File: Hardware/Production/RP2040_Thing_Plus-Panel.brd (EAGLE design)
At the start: 106.7 x 203.2 mm, 1590 parts, among them J1 SWD, J10 USB C, J11 microSD, J14 SWD, J15 Qwiic, J17 USB C, J18 microSD, J2 Qwiic, J21 SWD, J22 Qwiic, J24 USB C, J25 microSD, J28 SWD, J29 Qwiic, J3 Qwiic, J31 USB C, J32 microSD, J35 SWD, J36 Qwiic, J38 USB C, J39 microSD, J42 SWD, J43 Qwiic, J45 USB C, J46 microSD, J49 SWD, J5 USB C, J50 Qwiic, J52 USB C, J53 microSD, J56 SWD, J57 Qwiic, J59 USB C, J6 microSD, J60 microSD, J63 SWD, J64 Qwiic, J66 USB C, J67 microSD, J70 SWD, J71 Qwiic, J73 USB C, J74 microSD, J77 SWD, J78 Qwiic, J80 USB C, J81 microSD, J84 SWD, Q1 20V/4.2A/52mΩ/1.4W, Q10 20V/4.2A/52mΩ/1.4W, Q11 20V/4.2A/52mΩ/1.4W, Q12 20V/4.2A/52mΩ/1.4W, Q2 20V/4.2A/52mΩ/1.4W, Q3 20V/4.2A/52mΩ/1.4W, Q4 20V/4.2A/52mΩ/1.4W, Q5 20V/4.2A/52mΩ/1.4W, Q6 20V/4.2A/52mΩ/1.4W, Q7 20V/4.2A/52mΩ/1.4W, Q8 20V/4.2A/52mΩ/1.4W, Q9 20V/4.2A/52mΩ/1.4W, U1 W25QXX128MBIT, U10 WS2812-2020, U11 3.3V, U12 MCP73831, U13 W25QXX128MBIT, U14 RP2040, U15 MAX17048, U16 WS2812-2020, U17 3.3V, U18 MCP73831, U19 W25QXX128MBIT, U2 MAX17048, U20 RP2040, U21 MAX17048, U22 WS2812-2020, U23 3.3V, U24 MCP73831, U25 W25QXX128MBIT, U26 RP2040, U27 MAX17048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

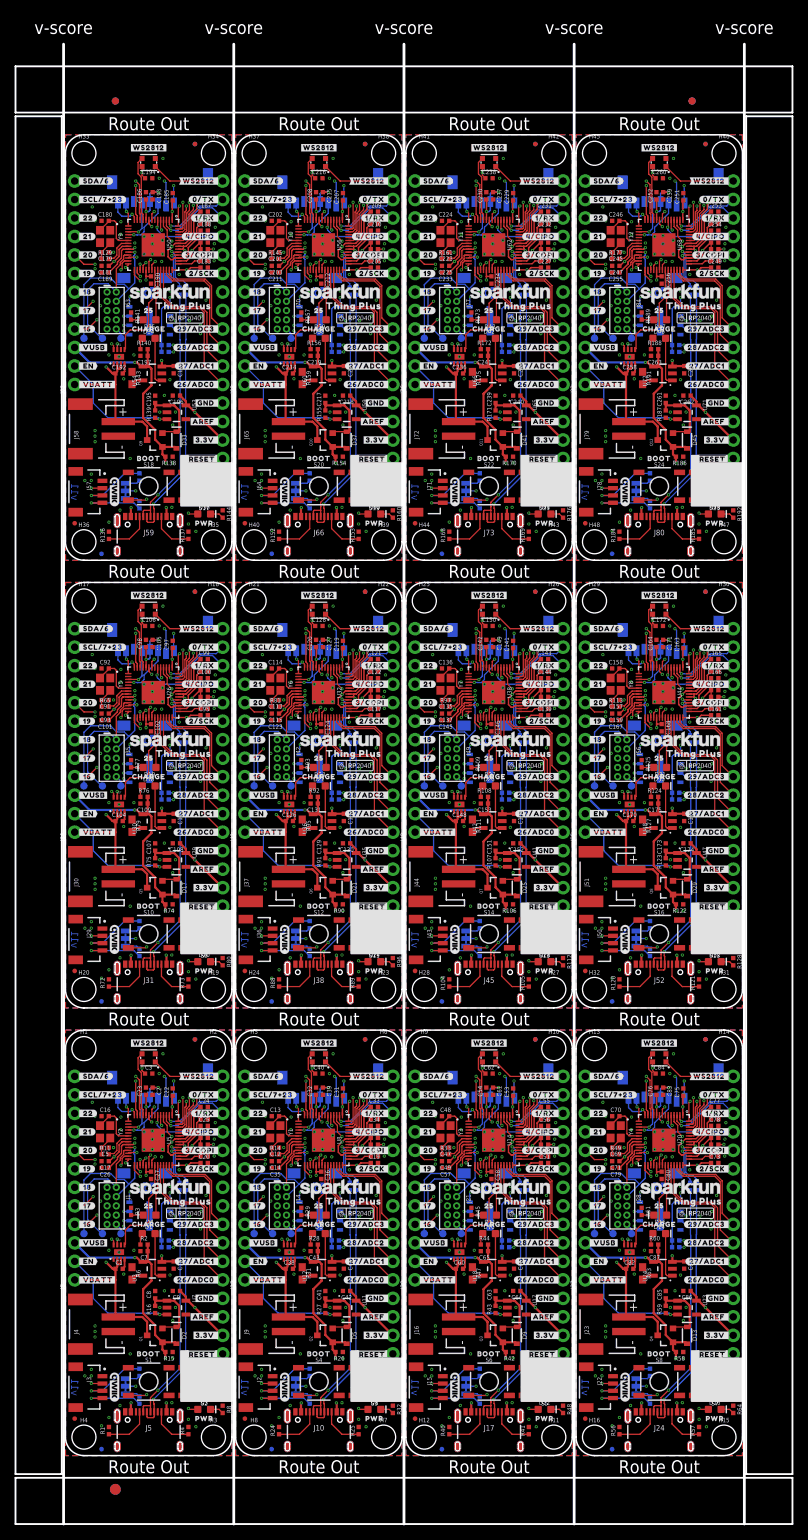
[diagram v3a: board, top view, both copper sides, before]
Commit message: Update RP2040 Logo
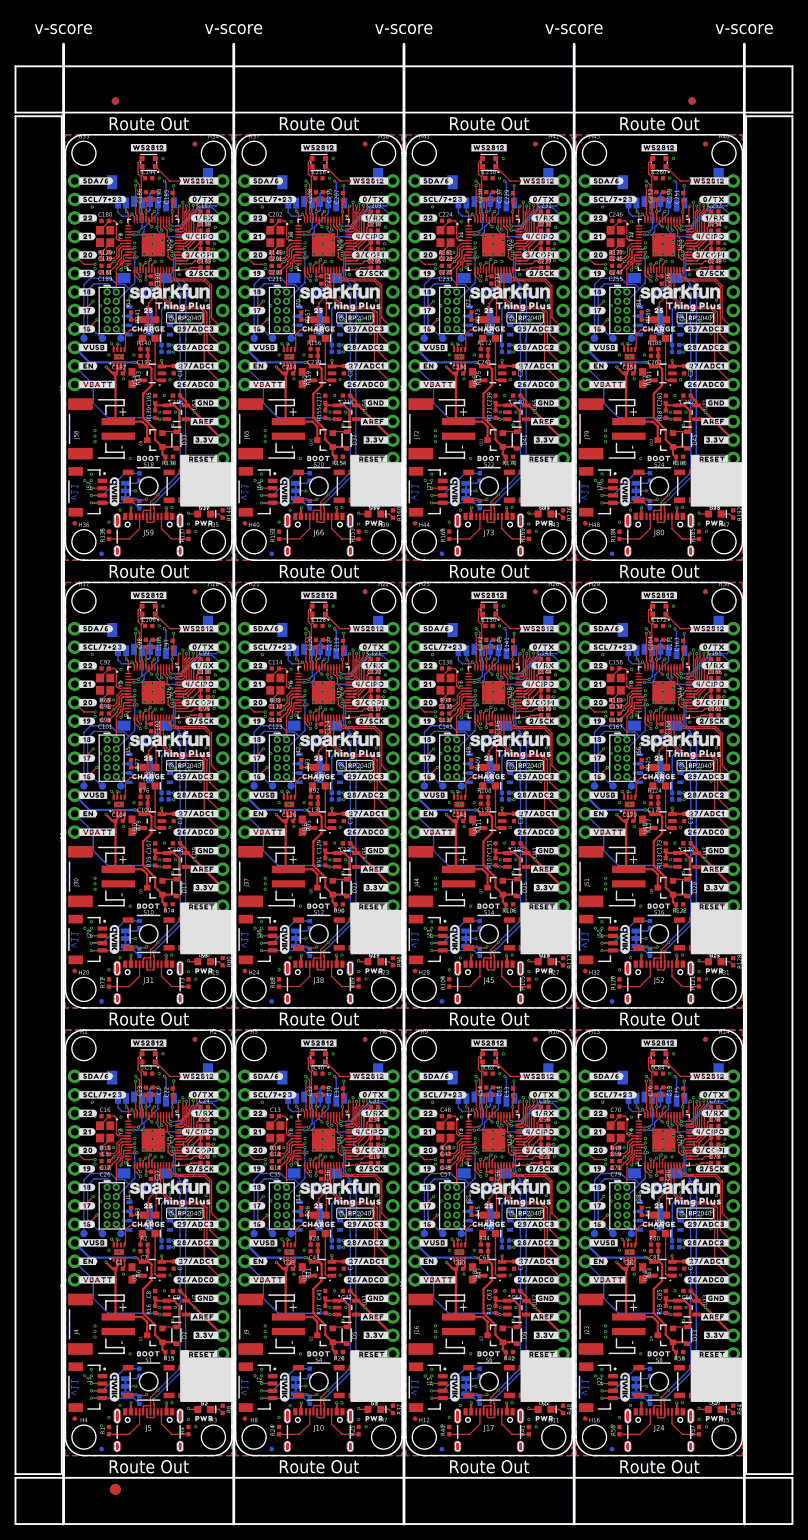
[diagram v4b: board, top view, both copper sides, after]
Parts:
- moved U$365 1.15 mm to (29.2, 75.9)
- moved U$426 1.15 mm to (52.6, 75.9)
- moved U$609 1.15 mm to (29.2, 137.4)
- moved U$670 1.15 mm to (52.6, 137.4)
- moved U$304 1.15 mm to (5.84, 75.9)
- moved U$548 1.15 mm to (5.84, 137.4)
- moved U$487 1.15 mm to (75.9, 75.9)
- moved U$731 1.15 mm to (75.9, 137.4)
- moved U$121 1.15 mm to (29.2, 14.5)
- moved U$182 1.15 mm to (52.6, 14.5)
- moved U$30 1.15 mm to (5.84, 14.5)
- moved U$243 1.15 mm to (75.9, 14.5)
- moved U$242 0.77 mm to (76.5, 17.1)
- moved U$486 0.77 mm to (76.5, 78.6)
- moved U$730 0.77 mm to (76.5, 140.1)
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
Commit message: Added ARM DevSummit Logo
Removed logos from bottom of PCB and replaced with ARM DevSummit logo.
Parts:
- removed U$709: (no value), output:#17_#0
- removed U$710: (no value), output:#16_#0
- removed U$711: (no value), output:#VUSB_#0
- removed U$712: (no value), output:#EN_#0
- removed U$713: (no value), output:#VBATT_#0
- removed U$714: (no value), output:#SCL_#0
- removed U$715: (no value), output:#SDA_#0
- removed U$716: (no value), output:#_#RESET##0
- removed U$717: (no value), output:#_3#3V#0
- removed U$718: (no value), output:#_AREF#0
- removed U$719: (no value), output:#_GND#0
- removed U$720: (no value), output:#_26#ADC0#0
- removed U$721: (no value), output:#_27#ADC1#0
- removed U$722: (no value), output:#_28#ADC2#0
- removed U$723: (no value), output:#_29#ADC3#0
- removed U$724, U$725: (no value), output:#_NC#0
- removed U$726: (no value), output:PWR0
- removed U$727: (no value), output:#I�C#0
- removed U$728: (no value), SparkFun-Aesthetics:SFE_LOGO_NAME_.1
- removed U$729: (no value), output:THING_PLUS_0
- removed U$730: (no value), output:THING_PLUS0
- removed U$731: (no value), RP2040:RP2040_20
- removed U$732: (no value), RP2040:RP2040_10
- U$100: device output:#16_#0 -> output:#VBATT_#0
- U$101: device output:#VUSB_#0 -> output:#SCL_#0
- U$102: device output:#EN_#0 -> output:#SDA_#0
- U$103: device output:#VBATT_#0 -> output:#_#RESET##0
- U$104: device output:#SCL_#0 -> output:#_3#3V#0
- U$105: device output:#SDA_#0 -> output:#_AREF#0
- U$106: device output:#_#RESET##0 -> output:#_GND#0
- U$107: device output:#_3#3V#0 -> output:#_26#ADC0#0
- U$108: device output:#_AREF#0 -> output:#_27#ADC1#0
- U$109: device output:#_GND#0 -> output:#_28#ADC2#0
- U$110: device output:#_26#ADC0#0 -> output:#_29#ADC3#0
- U$111: device output:#_27#ADC1#0 -> output:#_NC#0
- U$112: device output:#_28#ADC2#0 -> output:#_NC#0
- U$113: device output:#_29#ADC3#0 -> output:PWR0
- U$114: device output:#_NC#0 -> output:#I�C#0
- U$115: device output:#_NC#0 -> SparkFun-Aesthetics:SFE_LOGO_NAME_.1
- U$116: device output:PWR0 -> output:THING_PLUS_0
- U$117: device output:#I�C#0 -> RP2040:RP2040_10
- U$118: device SparkFun-Aesthetics:SFE_LOGO_NAME_.1 -> ARM1848_DevSummit_2021_Logos_ST3_Stacked#black#jpg (3):ARM1848_DEVSUMMIT_2021_LOGOS_ST3_STACKED#BLACK#JPG
- U$119: device output:THING_PLUS_0 -> output:#_16#0
- U$120: device output:THING_PLUS0 -> output:#_17#0
- U$121: device RP2040:RP2040_20 -> output:#_18#0
- U$122: device RP2040:RP2040_10 -> output:#_19#0
- U$123: device output:#_16#0 -> output:#_20#0
- U$124: device output:#_17#0 -> output:#_21#0
- U$125: device output:#_18#0 -> output:#_22#0
- U$126: device output:#_19#0 -> output:#WS2812_#0
- U$127: device output:#_20#0 -> output:#0#TX_#0
- U$128: device output:#_21#0 -> output:#1#RX_#0
- U$129: device output:#_22#0 -> output:#4#CIPO_#0
- U$130: device output:#WS2812_#0 -> output:#3#COPI_#0
- U$131: device output:#0#TX_#0 -> output:#2#SCK_#0
- U$132: device output:#1#RX_#0 -> output:#_SCL#7#23#0
- U$133: device output:#4#CIPO_#0 -> output:#_SDA#6#0
- U$134: device output:#3#COPI_#0 -> output:#29#ADC3_#0
- U$135: device output:#2#SCK_#0 -> output:#28#ADC2_#0
- U$136: device output:#_SCL#7#23#0 -> output:#27#ADC1_#0
- U$137: device output:#_SDA#6#0 -> output:#26#ADC0_#0
- U$138: device output:#29#ADC3_#0 -> output:#_VUSB#0
- U$139: device output:#28#ADC2_#0 -> output:#_EN#0
- U$140: device output:#27#ADC1_#0 -> output:#_VBATT#0
- U$141: device output:#26#ADC0_#0 -> output:#GND_#0
- U$142: device output:#_VUSB#0 -> output:#AREF_#0
- U$143: device output:#_EN#0 -> output:#3#3V_#0
- U$144: device output:#_VBATT#0 -> output:##RESET##0
- U$145: device output:#GND_#0 -> output:#WS2812#0
- U$146: device output:#AREF_#0 -> SparkFun-Aesthetics:QWIIC_4MM
- U$147: device output:#3#3V_#0 -> output:250
- U$148: device output:##RESET##0 -> output:CHARGE0
- U$149: device output:#WS2812#0 -> output:BOOT0
- U$150: device SparkFun-Aesthetics:QWIIC_4MM -> output:#22_#0
- U$151: device SparkFun-Aesthetics:SFE_LOGO_NAME_FLAME_.1 -> output:#21_#0
- U$152: device output:250 -> output:#20_#0
- U$153: device output:CHARGE0 -> output:#19_#0
- U$154: device output:BOOT0 -> output:#18_#0
- U$155: device output:#22_#0 -> output:#17_#0
- U$156: device output:#21_#0 -> output:#16_#0
- U$157: device output:#20_#0 -> output:#VUSB_#0
- U$158: device output:#19_#0 -> output:#EN_#0
- U$159: device output:#18_#0 -> output:#VBATT_#0
- U$160: device output:#17_#0 -> output:#SCL_#0
- U$161: device output:#16_#0 -> output:#SDA_#0
- U$162: device output:#VUSB_#0 -> output:#_#RESET##0
- U$163: device output:#EN_#0 -> output:#_3#3V#0
- U$164: device output:#VBATT_#0 -> output:#_AREF#0
- U$165: device output:#SCL_#0 -> output:#_GND#0
- U$166: device output:#SDA_#0 -> output:#_26#ADC0#0
- U$167: device output:#_#RESET##0 -> output:#_27#ADC1#0
- U$168: device output:#_3#3V#0 -> output:#_28#ADC2#0
- U$169: device output:#_AREF#0 -> output:#_29#ADC3#0
- U$170: device output:#_GND#0 -> output:#_NC#0
- U$171: device output:#_26#ADC0#0 -> output:#_NC#0
- U$172: device output:#_27#ADC1#0 -> output:PWR0
- U$173: device output:#_28#ADC2#0 -> output:#I�C#0
- U$174: device output:#_29#ADC3#0 -> SparkFun-Aesthetics:SFE_LOGO_NAME_.1
- U$175: device output:#_NC#0 -> output:THING_PLUS_0
- U$176: device output:#_NC#0 -> RP2040:RP2040_10
- U$177: device output:PWR0 -> ARM1848_DevSummit_2021_Logos_ST3_Stacked#black#jpg (3):ARM1848_DEVSUMMIT_2021_LOGOS_ST3_STACKED#BLACK#JPG
- U$178: device output:#I�C#0 -> output:#_16#0
- U$179: device SparkFun-Aesthetics:SFE_LOGO_NAME_.1 -> output:#_17#0
- U$180: device output:THING_PLUS_0 -> output:#_18#0
- U$181, U$44: device output:THING_PLUS0 -> output:#_19#0
- U$182: device RP2040:RP2040_20 -> output:#_20#0
- U$183: device RP2040:RP2040_10 -> output:#_21#0
- U$184: device output:#_16#0 -> output:#_22#0
- U$185: device output:#_17#0 -> output:#WS2812_#0
- U$186: device output:#_18#0 -> output:#0#TX_#0
- U$187: device output:#_19#0 -> output:#1#RX_#0
- U$188: device output:#_20#0 -> output:#4#CIPO_#0
- U$189: device output:#_21#0 -> output:#3#COPI_#0
- U$190: device output:#_22#0 -> output:#2#SCK_#0
- U$191: device output:#WS2812_#0 -> output:#_SCL#7#23#0
- U$192: device output:#0#TX_#0 -> output:#_SDA#6#0
- U$193: device output:#1#RX_#0 -> output:#29#ADC3_#0
- U$194: device output:#4#CIPO_#0 -> output:#28#ADC2_#0
- U$195: device output:#3#COPI_#0 -> output:#27#ADC1_#0
- U$196: device output:#2#SCK_#0 -> output:#26#ADC0_#0
- U$197: device output:#_SCL#7#23#0 -> output:#_VUSB#0
- U$198: device output:#_SDA#6#0 -> output:#_EN#0
- U$199: device output:#29#ADC3_#0 -> output:#_VBATT#0
- U$200: device output:#28#ADC2_#0 -> output:#GND_#0
- U$201: device output:#27#ADC1_#0 -> output:#AREF_#0
- U$202: device output:#26#ADC0_#0 -> output:#3#3V_#0
- U$203: device output:#_VUSB#0 -> output:##RESET##0
- U$204: device output:#_EN#0 -> output:#WS2812#0
- U$205: device output:#_VBATT#0 -> SparkFun-Aesthetics:QWIIC_4MM
- U$206: device output:#GND_#0 -> output:250
- U$207: device output:#AREF_#0 -> output:CHARGE0
- U$208: device output:#3#3V_#0 -> output:BOOT0
- U$209: device output:##RESET##0 -> output:#22_#0
- U$210: device output:#WS2812#0 -> output:#21_#0
- U$211: device SparkFun-Aesthetics:QWIIC_4MM -> output:#20_#0
- U$212: device SparkFun-Aesthetics:SFE_LOGO_NAME_FLAME_.1 -> output:#19_#0
- U$213: device output:250 -> output:#18_#0
- U$214: device output:CHARGE0 -> output:#17_#0
- U$215: device output:BOOT0 -> output:#16_#0
- U$216: device output:#22_#0 -> output:#VUSB_#0
- U$217: device output:#21_#0 -> output:#EN_#0
- U$218: device output:#20_#0 -> output:#VBATT_#0
- U$219: device output:#19_#0 -> output:#SCL_#0
- U$220: device output:#18_#0 -> output:#SDA_#0
- U$221: device output:#17_#0 -> output:#_#RESET##0
- U$222: device output:#16_#0 -> output:#_3#3V#0
- U$223: device output:#VUSB_#0 -> output:#_AREF#0
- U$224: device output:#EN_#0 -> output:#_GND#0
- U$225: device output:#VBATT_#0 -> output:#_26#ADC0#0
- U$226: device output:#SCL_#0 -> output:#_27#ADC1#0
- U$227: device output:#SDA_#0 -> output:#_28#ADC2#0
- U$228: device output:#_#RESET##0 -> output:#_29#ADC3#0
- U$229: device output:#_3#3V#0 -> output:#_NC#0
- U$230: device output:#_AREF#0 -> output:#_NC#0
- U$231: device output:#_GND#0 -> output:PWR0
- U$232: device output:#_26#ADC0#0 -> output:#I�C#0
- U$233: device output:#_27#ADC1#0 -> SparkFun-Aesthetics:SFE_LOGO_NAME_.1
- U$234: device output:#_28#ADC2#0 -> output:THING_PLUS_0
- U$235: device output:#_29#ADC3#0 -> RP2040:RP2040_10
- U$236: device output:#_NC#0 -> ARM1848_DevSummit_2021_Logos_ST3_Stacked#black#jpg (3):ARM1848_DEVSUMMIT_2021_LOGOS_ST3_STACKED#BLACK#JPG
- U$237: device output:#_NC#0 -> output:#_16#0
- U$238: device output:PWR0 -> output:#_17#0
- U$239: device output:#I�C#0 -> output:#_18#0
- U$240: device SparkFun-Aesthetics:SFE_LOGO_NAME_.1 -> output:#_19#0
- U$241: device output:THING_PLUS_0 -> output:#_20#0
- U$242: device output:THING_PLUS0 -> output:#_21#0
- U$243: device RP2040:RP2040_20 -> output:#_22#0
- U$244: device RP2040:RP2040_10 -> output:#WS2812_#0
- U$245: device output:#_16#0 -> output:#0#TX_#0
- U$246: device output:#_17#0 -> output:#1#RX_#0
- U$247: device output:#_18#0 -> output:#4#CIPO_#0
- U$248: device output:#_19#0 -> output:#3#COPI_#0
- U$249: device output:#_20#0 -> output:#2#SCK_#0
- U$250: device output:#_21#0 -> output:#_SCL#7#23#0
- U$251: device output:#_22#0 -> output:#_SDA#6#0
- U$252: device output:#WS2812_#0 -> output:#29#ADC3_#0
- U$253: device output:#0#TX_#0 -> output:#28#ADC2_#0
- U$254: device output:#1#RX_#0 -> output:#27#ADC1_#0
- U$255: device output:#4#CIPO_#0 -> output:#26#ADC0_#0
- U$256: device output:#3#COPI_#0 -> output:#_VUSB#0
- U$257: device output:#2#SCK_#0 -> output:#_EN#0
- U$258: device output:#_SCL#7#23#0 -> output:#_VBATT#0
- U$259: device output:#_SDA#6#0 -> output:#GND_#0
- U$260: device output:#29#ADC3_#0 -> output:#AREF_#0
- U$261: device output:#28#ADC2_#0 -> output:#3#3V_#0
- U$262: device output:#27#ADC1_#0 -> output:##RESET##0
- U$263: device output:#26#ADC0_#0 -> output:#WS2812#0
- U$264: device output:#_VUSB#0 -> SparkFun-Aesthetics:QWIIC_4MM
- U$265: device output:#_EN#0 -> output:250
- U$266: device output:#_VBATT#0 -> output:CHARGE0
- U$267: device output:#GND_#0 -> output:BOOT0
- U$268: device output:#AREF_#0 -> output:#22_#0
- U$269: device output:#3#3V_#0 -> output:#21_#0
- U$270: device output:##RESET##0 -> output:#20_#0
- U$271: device output:#WS2812#0 -> output:#19_#0
- U$272: device SparkFun-Aesthetics:QWIIC_4MM -> output:#18_#0
- U$273: device SparkFun-Aesthetics:SFE_LOGO_NAME_FLAME_.1 -> output:#17_#0
- U$274: device output:250 -> output:#16_#0
- U$275: device output:CHARGE0 -> output:#VUSB_#0
- U$276: device output:BOOT0 -> output:#EN_#0
- U$277: device output:#22_#0 -> output:#VBATT_#0
- U$278: device output:#21_#0 -> output:#SCL_#0
- U$279: device output:#20_#0 -> output:#SDA_#0
- U$280: device output:#19_#0 -> output:#_#RESET##0
- U$281: device output:#18_#0 -> output:#_3#3V#0
- U$282: device output:#17_#0 -> output:#_AREF#0
- U$283: device output:#16_#0 -> output:#_GND#0
- U$284: device output:#VUSB_#0 -> output:#_26#ADC0#0
- U$285: device output:#EN_#0 -> output:#_27#ADC1#0
- U$286: device output:#VBATT_#0 -> output:#_28#ADC2#0
- U$287: device output:#SCL_#0 -> output:#_29#ADC3#0
- U$288: device output:#SDA_#0 -> output:#_NC#0
- U$289: device output:#_#RESET##0 -> output:#_NC#0
- U$290: device output:#_3#3V#0 -> output:PWR0
- U$291: device output:#_AREF#0 -> output:#I�C#0
- U$292: device output:#_GND#0 -> SparkFun-Aesthetics:SFE_LOGO_NAME_.1
- U$293: device output:#_26#ADC0#0 -> output:THING_PLUS_0
- U$294: device output:#_27#ADC1#0 -> RP2040:RP2040_10
- U$295: device output:#_28#ADC2#0 -> ARM1848_DevSummit_2021_Logos_ST3_Stacked#black#jpg (3):ARM1848_DEVSUMMIT_2021_LOGOS_ST3_STACKED#BLACK#JPG
- U$296: device output:#_29#ADC3#0 -> output:#_16#0
- U$297: device output:#_NC#0 -> output:#_17#0
- U$298: device output:#_NC#0 -> output:#_18#0
- U$299: device output:PWR0 -> output:#_19#0
- U$30: device RP2040:RP2040_20 -> ARM1848_DevSummit_2021_Logos_ST3_Stacked#black#jpg (3):ARM1848_DEVSUMMIT_2021_LOGOS_ST3_STACKED#BLACK#JPG
- U$300: device output:#I�C#0 -> output:#_20#0
- U$301: device SparkFun-Aesthetics:SFE_LOGO_NAME_.1 -> output:#_21#0
- U$302: device output:THING_PLUS_0 -> output:#_22#0
- U$303: device output:THING_PLUS0 -> output:#WS2812_#0
- U$304: device RP2040:RP2040_20 -> output:#0#TX_#0
- U$305: device RP2040:RP2040_10 -> output:#1#RX_#0
- U$306: device output:#_16#0 -> output:#4#CIPO_#0
- U$307: device output:#_17#0 -> output:#3#COPI_#0
- U$308: device output:#_18#0 -> output:#2#SCK_#0
- U$309: device output:#_19#0 -> output:#_SCL#7#23#0
- U$310: device output:#_20#0 -> output:#_SDA#6#0
- U$311: device output:#_21#0 -> output:#29#ADC3_#0
- U$312: device output:#_22#0 -> output:#28#ADC2_#0
- U$313: device output:#WS2812_#0 -> output:#27#ADC1_#0
- U$314: device output:#0#TX_#0 -> output:#26#ADC0_#0
- U$315: device output:#1#RX_#0 -> output:#_VUSB#0
- U$316: device output:#4#CIPO_#0 -> output:#_EN#0
- U$317: device output:#3#COPI_#0 -> output:#_VBATT#0
- U$318: device output:#2#SCK_#0 -> output:#GND_#0
- U$319: device output:#_SCL#7#23#0 -> output:#AREF_#0
- U$32: device SparkFun-Aesthetics:SFE_LOGO_NAME_FLAME_.1 -> output:#_17#0
- U$320: device output:#_SDA#6#0 -> output:#3#3V_#0
- U$321: device output:#29#ADC3_#0 -> output:##RESET##0
- U$322: device output:#28#ADC2_#0 -> output:#WS2812#0
- U$323: device output:#27#ADC1_#0 -> SparkFun-Aesthetics:QWIIC_4MM
- U$324: device output:#26#ADC0_#0 -> output:250
- U$325: device output:#_VUSB#0 -> output:CHARGE0
- U$326: device output:#_EN#0 -> output:BOOT0
- U$327: device output:#_VBATT#0 -> output:#22_#0
- U$328: device output:#GND_#0 -> output:#21_#0
- U$329: device output:#AREF_#0 -> output:#20_#0
- U$330: device output:#3#3V_#0 -> output:#19_#0
- U$331: device output:##RESET##0 -> output:#18_#0
- U$332: device output:#WS2812#0 -> output:#17_#0
- U$333: device SparkFun-Aesthetics:QWIIC_4MM -> output:#16_#0
- U$334: device SparkFun-Aesthetics:SFE_LOGO_NAME_FLAME_.1 -> output:#VUSB_#0
- U$335: device output:250 -> output:#EN_#0
- U$336: device output:CHARGE0 -> output:#VBATT_#0
- U$337: device output:BOOT0 -> output:#SCL_#0
- U$338: device output:#22_#0 -> output:#SDA_#0
- U$339: device output:#21_#0 -> output:#_#RESET##0
- U$340: device output:#20_#0 -> output:#_3#3V#0
- U$341: device output:#19_#0 -> output:#_AREF#0
- U$342: device output:#18_#0 -> output:#_GND#0
- U$343: device output:#17_#0 -> output:#_26#ADC0#0
- U$344: device output:#16_#0 -> output:#_27#ADC1#0
- U$345: device output:#VUSB_#0 -> output:#_28#ADC2#0
- U$346: device output:#EN_#0 -> output:#_29#ADC3#0
- U$347: device output:#VBATT_#0 -> output:#_NC#0
- U$348: device output:#SCL_#0 -> output:#_NC#0
- U$349: device output:#SDA_#0 -> output:PWR0
- U$350: device output:#_#RESET##0 -> output:#I�C#0
- U$351: device output:#_3#3V#0 -> SparkFun-Aesthetics:SFE_LOGO_NAME_.1
- U$352: device output:#_AREF#0 -> output:THING_PLUS_0
- U$353: device output:#_GND#0 -> RP2040:RP2040_10
- U$354: device output:#_26#ADC0#0 -> ARM1848_DevSummit_2021_Logos_ST3_Stacked#black#jpg (3):ARM1848_DEVSUMMIT_2021_LOGOS_ST3_STACKED#BLACK#JPG
- U$355: device output:#_27#ADC1#0 -> output:#_16#0
- U$356: device output:#_28#ADC2#0 -> output:#_17#0
- U$357: device output:#_29#ADC3#0 -> output:#_18#0
- U$358: device output:#_NC#0 -> output:#_19#0
- U$359: device output:#_NC#0 -> output:#_20#0
- U$360: device output:PWR0 -> output:#_21#0
- U$361: device output:#I�C#0 -> output:#_22#0
- U$362: device SparkFun-Aesthetics:SFE_LOGO_NAME_.1 -> output:#WS2812_#0
- U$363: device output:THING_PLUS_0 -> output:#0#TX_#0
- U$364: device output:THING_PLUS0 -> output:#1#RX_#0
- U$365: device RP2040:RP2040_20 -> output:#4#CIPO_#0
- U$366: device RP2040:RP2040_10 -> output:#3#COPI_#0
- U$367: device output:#_16#0 -> output:#2#SCK_#0
- U$368: device output:#_17#0 -> output:#_SCL#7#23#0
- U$369: device output:#_18#0 -> output:#_SDA#6#0
- U$370: device output:#_19#0 -> output:#29#ADC3_#0
- U$371: device output:#_20#0 -> output:#28#ADC2_#0
- U$372: device output:#_21#0 -> output:#27#ADC1_#0
- U$373: device output:#_22#0 -> output:#26#ADC0_#0
- U$374: device output:#WS2812_#0 -> output:#_VUSB#0
- U$375: device output:#0#TX_#0 -> output:#_EN#0
- U$376: device output:#1#RX_#0 -> output:#_VBATT#0
- U$377: device output:#4#CIPO_#0 -> output:#GND_#0
- U$378: device output:#3#COPI_#0 -> output:#AREF_#0
- U$379: device output:#2#SCK_#0 -> output:#3#3V_#0
- U$380: device output:#_SCL#7#23#0 -> output:##RESET##0
- U$381: device output:#_SDA#6#0 -> output:#WS2812#0
- U$382: device output:#29#ADC3_#0 -> SparkFun-Aesthetics:QWIIC_4MM
- U$383: device output:#28#ADC2_#0 -> output:250
- U$384: device output:#27#ADC1_#0 -> output:CHARGE0
- U$385: device output:#26#ADC0_#0 -> output:BOOT0
- U$386: device output:#_VUSB#0 -> output:#22_#0
- U$387: device output:#_EN#0 -> output:#21_#0
- U$388: device output:#_VBATT#0 -> output:#20_#0
- U$389: device output:#GND_#0 -> output:#19_#0
- U$390: device output:#AREF_#0 -> output:#18_#0
- U$391: device output:#3#3V_#0 -> output:#17_#0
- U$392: device output:##RESET##0 -> output:#16_#0
- U$393: device output:#WS2812#0 -> output:#VUSB_#0
- U$394: device SparkFun-Aesthetics:QWIIC_4MM -> output:#EN_#0
- U$395: device SparkFun-Aesthetics:SFE_LOGO_NAME_FLAME_.1 -> output:#VBATT_#0
- U$396: device output:250 -> output:#SCL_#0
- U$397: device output:CHARGE0 -> output:#SDA_#0
- U$398: device output:BOOT0 -> output:#_#RESET##0
- U$399: device output:#22_#0 -> output:#_3#3V#0
- U$400: device output:#21_#0 -> output:#_AREF#0
- U$401: device output:#20_#0 -> output:#_GND#0
- U$402: device output:#19_#0 -> output:#_26#ADC0#0
- U$403: device output:#18_#0 -> output:#_27#ADC1#0
- U$404: device output:#17_#0 -> output:#_28#ADC2#0
- U$405: device output:#16_#0 -> output:#_29#ADC3#0
- U$406: device output:#VUSB_#0 -> output:#_NC#0
- U$407: device output:#EN_#0 -> output:#_NC#0
- U$408: device output:#VBATT_#0 -> output:PWR0
- U$409: device output:#SCL_#0 -> output:#I�C#0
- U$410: device output:#SDA_#0 -> SparkFun-Aesthetics:SFE_LOGO_NAME_.1
- U$411: device output:#_#RESET##0 -> output:THING_PLUS_0
- U$412: device output:#_3#3V#0 -> RP2040:RP2040_10
- U$413: device output:#_AREF#0 -> ARM1848_DevSummit_2021_Logos_ST3_Stacked#black#jpg (3):ARM1848_DEVSUMMIT_2021_LOGOS_ST3_STACKED#BLACK#JPG
- U$414: device output:#_GND#0 -> output:#_16#0
- U$415: device output:#_26#ADC0#0 -> output:#_17#0
- U$416: device output:#_27#ADC1#0 -> output:#_18#0
- U$417: device output:#_28#ADC2#0 -> output:#_19#0
- U$418: device output:#_29#ADC3#0 -> output:#_20#0
- U$419: device output:#_NC#0 -> output:#_21#0
- U$420: device output:#_NC#0 -> output:#_22#0
- U$421: device output:PWR0 -> output:#WS2812_#0
- U$422: device output:#I�C#0 -> output:#0#TX_#0
- U$423: device SparkFun-Aesthetics:SFE_LOGO_NAME_.1 -> output:#1#RX_#0
- U$424: device output:THING_PLUS_0 -> output:#4#CIPO_#0
- U$425: device output:THING_PLUS0 -> output:#3#COPI_#0
- U$426: device RP2040:RP2040_20 -> output:#2#SCK_#0
- U$427: device RP2040:RP2040_10 -> output:#_SCL#7#23#0
- U$428: device output:#_16#0 -> output:#_SDA#6#0
- U$429: device output:#_17#0 -> output:#29#ADC3_#0
- U$43: device output:#_17#0 -> output:#_18#0
- U$430: device output:#_18#0 -> output:#28#ADC2_#0
- U$431: device output:#_19#0 -> output:#27#ADC1_#0
- U$432: device output:#_20#0 -> output:#26#ADC0_#0
- U$433: device output:#_21#0 -> output:#_VUSB#0
- U$434: device output:#_22#0 -> output:#_EN#0
- U$435: device output:#WS2812_#0 -> output:#_VBATT#0
- U$436: device output:#0#TX_#0 -> output:#GND_#0
- U$437: device output:#1#RX_#0 -> output:#AREF_#0
- U$438: device output:#4#CIPO_#0 -> output:#3#3V_#0
- U$439: device output:#3#COPI_#0 -> output:##RESET##0
- U$440: device output:#2#SCK_#0 -> output:#WS2812#0
- U$441: device output:#_SCL#7#23#0 -> SparkFun-Aesthetics:QWIIC_4MM
- U$442: device output:#_SDA#6#0 -> output:250
- U$443: device output:#29#ADC3_#0 -> output:CHARGE0
- U$444: device output:#28#ADC2_#0 -> output:BOOT0
- U$445: device output:#27#ADC1_#0 -> output:#22_#0
- U$446: device output:#26#ADC0_#0 -> output:#21_#0
- U$447: device output:#_VUSB#0 -> output:#20_#0
- U$448: device output:#_EN#0 -> output:#19_#0
- U$449: device output:#_VBATT#0 -> output:#18_#0
- U$450: device output:#GND_#0 -> output:#17_#0
- U$451: device output:#AREF_#0 -> output:#16_#0
- U$452: device output:#3#3V_#0 -> output:#VUSB_#0
- U$453: device output:##RESET##0 -> output:#EN_#0
- U$454: device output:#WS2812#0 -> output:#VBATT_#0
- U$455: device SparkFun-Aesthetics:QWIIC_4MM -> output:#SCL_#0
- U$456: device SparkFun-Aesthetics:SFE_LOGO_NAME_FLAME_.1 -> output:#SDA_#0
- U$457: device output:250 -> output:#_#RESET##0
- U$458: device output:CHARGE0 -> output:#_3#3V#0
- U$459: device output:BOOT0 -> output:#_AREF#0
- U$46: device output:#_18#0 -> output:#_20#0
- U$460: device output:#22_#0 -> output:#_GND#0
- U$461: device output:#21_#0 -> output:#_26#ADC0#0
- U$462: device output:#20_#0 -> output:#_27#ADC1#0
- U$463: device output:#19_#0 -> output:#_28#ADC2#0
- U$464: device output:#18_#0 -> output:#_29#ADC3#0
- U$465: device output:#17_#0 -> output:#_NC#0
- U$466: device output:#16_#0 -> output:#_NC#0
- U$467: device output:#VUSB_#0 -> output:PWR0
- U$468: device output:#EN_#0 -> output:#I�C#0
- U$469: device output:#VBATT_#0 -> SparkFun-Aesthetics:SFE_LOGO_NAME_.1
- U$470: device output:#SCL_#0 -> output:THING_PLUS_0
- U$471: device output:#SDA_#0 -> RP2040:RP2040_10
- U$472: device output:#_#RESET##0 -> ARM1848_DevSummit_2021_Logos_ST3_Stacked#black#jpg (3):ARM1848_DEVSUMMIT_2021_LOGOS_ST3_STACKED#BLACK#JPG
- U$473: device output:#_3#3V#0 -> output:#_16#0
- U$474: device output:#_AREF#0 -> output:#_17#0
- U$475: device output:#_GND#0 -> output:#_18#0
- U$476: device output:#_26#ADC0#0 -> output:#_19#0
- U$477: device output:#_27#ADC1#0 -> output:#_20#0
- U$478: device output:#_28#ADC2#0 -> output:#_21#0
- U$479: device output:#_29#ADC3#0 -> output:#_22#0
- U$48: device output:#_19#0 -> output:#_21#0
- U$480: device output:#_NC#0 -> output:#WS2812_#0
- U$481: device output:#_NC#0 -> output:#0#TX_#0
- U$482: device output:PWR0 -> output:#1#RX_#0
- U$483: device output:#I�C#0 -> output:#4#CIPO_#0
- U$484: device SparkFun-Aesthetics:SFE_LOGO_NAME_.1 -> output:#3#COPI_#0
- U$485: device output:THING_PLUS_0 -> output:#2#SCK_#0
- U$486: device output:THING_PLUS0 -> output:#_SCL#7#23#0
- U$487: device RP2040:RP2040_20 -> output:#_SDA#6#0
- U$488: device RP2040:RP2040_10 -> output:#29#ADC3_#0
- U$489: device output:#_16#0 -> output:#28#ADC2_#0
- U$49: device output:#_20#0 -> output:#_22#0
- U$490: device output:#_17#0 -> output:#27#ADC1_#0
- U$491: device output:#_18#0 -> output:#26#ADC0_#0
- U$492: device output:#_19#0 -> output:#_VUSB#0
- U$493: device output:#_20#0 -> output:#_EN#0
- U$494: device output:#_21#0 -> output:#_VBATT#0
- U$495: device output:#_22#0 -> output:#GND_#0
- U$496: device output:#WS2812_#0 -> output:#AREF_#0
- U$497: device output:#0#TX_#0 -> output:#3#3V_#0
- U$498: device output:#1#RX_#0 -> output:##RESET##0
- U$499: device output:#4#CIPO_#0 -> output:#WS2812#0
- U$50: device output:#_21#0 -> output:#WS2812_#0
- U$500: device output:#3#COPI_#0 -> SparkFun-Aesthetics:QWIIC_4MM
- U$501: device output:#2#SCK_#0 -> output:250
- U$502: device output:#_SCL#7#23#0 -> output:CHARGE0
- U$503: device output:#_SDA#6#0 -> output:BOOT0
- U$504: device output:#29#ADC3_#0 -> output:#22_#0
- U$505: device output:#28#ADC2_#0 -> output:#21_#0
- U$506: device output:#27#ADC1_#0 -> output:#20_#0
- U$507: device output:#26#ADC0_#0 -> output:#19_#0
- U$508: device output:#_VUSB#0 -> output:#18_#0
- U$509: device output:#_EN#0 -> output:#17_#0
- U$51: device output:#_22#0 -> output:#0#TX_#0
- U$510: device output:#_VBATT#0 -> output:#16_#0
- U$511: device output:#GND_#0 -> output:#VUSB_#0
- U$512: device output:#AREF_#0 -> output:#EN_#0
- U$513: device output:#3#3V_#0 -> output:#VBATT_#0
- U$514: device output:##RESET##0 -> output:#SCL_#0
- U$515: device output:#WS2812#0 -> output:#SDA_#0
- U$516: device SparkFun-Aesthetics:QWIIC_4MM -> output:#_#RESET##0
- U$517: device SparkFun-Aesthetics:SFE_LOGO_NAME_FLAME_.1 -> output:#_3#3V#0
- U$518: device output:250 -> output:#_AREF#0
- U$519: device output:CHARGE0 -> output:#_GND#0
- U$52: device output:#WS2812_#0 -> output:#1#RX_#0
- U$520: device output:BOOT0 -> output:#_26#ADC0#0
- U$521: device output:#22_#0 -> output:#_27#ADC1#0
- U$522: device output:#21_#0 -> output:#_28#ADC2#0
- U$523: device output:#20_#0 -> output:#_29#ADC3#0
- U$524: device output:#19_#0 -> output:#_NC#0
- U$525: device output:#18_#0 -> output:#_NC#0
- U$526: device output:#17_#0 -> output:PWR0
- U$527: device output:#16_#0 -> output:#I�C#0
- U$528: device output:#VUSB_#0 -> SparkFun-Aesthetics:SFE_LOGO_NAME_.1
- U$529: device output:#EN_#0 -> output:THING_PLUS_0
- U$53: device output:#0#TX_#0 -> output:#4#CIPO_#0
- U$530: device output:#VBATT_#0 -> RP2040:RP2040_10
- U$531: device output:#SCL_#0 -> ARM1848_DevSummit_2021_Logos_ST3_Stacked#black#jpg (3):ARM1848_DEVSUMMIT_2021_LOGOS_ST3_STACKED#BLACK#JPG
- U$532: device output:#SDA_#0 -> output:#_16#0
- U$533: device output:#_#RESET##0 -> output:#_17#0
- U$534: device output:#_3#3V#0 -> output:#_18#0
- U$535: device output:#_AREF#0 -> output:#_19#0
- U$536: device output:#_GND#0 -> output:#_20#0
- U$537: device output:#_26#ADC0#0 -> output:#_21#0
- U$538: device output:#_27#ADC1#0 -> output:#_22#0
- U$539: device output:#_28#ADC2#0 -> output:#WS2812_#0
- U$540: device output:#_29#ADC3#0 -> output:#0#TX_#0
- U$541: device output:#_NC#0 -> output:#1#RX_#0
- U$542: device output:#_NC#0 -> output:#4#CIPO_#0
- U$543: device output:PWR0 -> output:#3#COPI_#0
- U$544: device output:#I�C#0 -> output:#2#SCK_#0
- U$545: device SparkFun-Aesthetics:SFE_LOGO_NAME_.1 -> output:#_SCL#7#23#0
- U$546: device output:THING_PLUS_0 -> output:#_SDA#6#0
- U$547: device output:THING_PLUS0 -> output:#29#ADC3_#0
- U$548: device RP2040:RP2040_20 -> output:#28#ADC2_#0
- U$549: device RP2040:RP2040_10 -> output:#27#ADC1_#0
- U$550: device output:#_16#0 -> output:#26#ADC0_#0
- U$551: device output:#_17#0 -> output:#_VUSB#0
- U$552: device output:#_18#0 -> output:#_EN#0
- U$553: device output:#_19#0 -> output:#_VBATT#0
- U$554: device output:#_20#0 -> output:#GND_#0
- U$555: device output:#_21#0 -> output:#AREF_#0
- U$556: device output:#_22#0 -> output:#3#3V_#0
- U$557: device output:#WS2812_#0 -> output:##RESET##0
- U$558: device output:#0#TX_#0 -> output:#WS2812#0
- U$559: device output:#1#RX_#0 -> SparkFun-Aesthetics:QWIIC_4MM
- U$560: device output:#4#CIPO_#0 -> output:250
- U$561: device output:#3#COPI_#0 -> output:CHARGE0
- U$562: device output:#2#SCK_#0 -> output:BOOT0
- U$563: device output:#_SCL#7#23#0 -> output:#22_#0
- U$564: device output:#_SDA#6#0 -> output:#21_#0
- U$565: device output:#29#ADC3_#0 -> output:#20_#0
- U$566: device output:#28#ADC2_#0 -> output:#19_#0
- U$567: device output:#27#ADC1_#0 -> output:#18_#0
- U$568: device output:#26#ADC0_#0 -> output:#17_#0
- U$569: device output:#_VUSB#0 -> output:#16_#0
- U$570: device output:#_EN#0 -> output:#VUSB_#0
- U$571: device output:#_VBATT#0 -> output:#EN_#0
- U$572: device output:#GND_#0 -> output:#VBATT_#0
- U$573: device output:#AREF_#0 -> output:#SCL_#0
- U$574: device output:#3#3V_#0 -> output:#SDA_#0
- U$575: device output:##RESET##0 -> output:#_#RESET##0
- U$576: device output:#WS2812#0 -> output:#_3#3V#0
- U$577: device SparkFun-Aesthetics:QWIIC_4MM -> output:#_AREF#0
- U$578: device SparkFun-Aesthetics:SFE_LOGO_NAME_FLAME_.1 -> output:#_GND#0
- U$579: device output:250 -> output:#_26#ADC0#0
- U$580: device output:CHARGE0 -> output:#_27#ADC1#0
- U$581: device output:BOOT0 -> output:#_28#ADC2#0
- U$582: device output:#22_#0 -> output:#_29#ADC3#0
- U$583: device output:#21_#0 -> output:#_NC#0
- U$584: device output:#20_#0 -> output:#_NC#0
- U$585: device output:#19_#0 -> output:PWR0
- U$586: device output:#18_#0 -> output:#I�C#0
- U$587: device output:#17_#0 -> SparkFun-Aesthetics:SFE_LOGO_NAME_.1
- U$588: device output:#16_#0 -> output:THING_PLUS_0
- U$589: device output:#VUSB_#0 -> RP2040:RP2040_10
- U$590: device output:#EN_#0 -> ARM1848_DevSummit_2021_Logos_ST3_Stacked#black#jpg (3):ARM1848_DEVSUMMIT_2021_LOGOS_ST3_STACKED#BLACK#JPG
- U$591: device output:#VBATT_#0 -> output:#_16#0
- U$592: device output:#SCL_#0 -> output:#_17#0
- U$593: device output:#SDA_#0 -> output:#_18#0
- U$594: device output:#_#RESET##0 -> output:#_19#0
- U$595: device output:#_3#3V#0 -> output:#_20#0
- U$596: device output:#_AREF#0 -> output:#_21#0
- U$597: device output:#_GND#0 -> output:#_22#0
- U$598: device output:#_26#ADC0#0 -> output:#WS2812_#0
- U$599: device output:#_27#ADC1#0 -> output:#0#TX_#0
- U$600: device output:#_28#ADC2#0 -> output:#1#RX_#0
- U$601: device output:#_29#ADC3#0 -> output:#4#CIPO_#0
- U$602: device output:#_NC#0 -> output:#3#COPI_#0
- U$603: device output:#_NC#0 -> output:#2#SCK_#0
- U$604: device output:PWR0 -> output:#_SCL#7#23#0
- U$605: device output:#I�C#0 -> output:#_SDA#6#0
- U$606: device SparkFun-Aesthetics:SFE_LOGO_NAME_.1 -> output:#29#ADC3_#0
- U$607: device output:THING_PLUS_0 -> output:#28#ADC2_#0
- U$608: device output:THING_PLUS0 -> output:#27#ADC1_#0
- U$609: device RP2040:RP2040_20 -> output:#26#ADC0_#0
- U$610: device RP2040:RP2040_10 -> output:#_VUSB#0
- U$611: device output:#_16#0 -> output:#_EN#0
- U$612: device output:#_17#0 -> output:#_VBATT#0
- U$613: device output:#_18#0 -> output:#GND_#0
- U$614: device output:#_19#0 -> output:#AREF_#0
- U$615: device output:#_20#0 -> output:#3#3V_#0
- U$616: device output:#_21#0 -> output:##RESET##0
- U$617: device output:#_22#0 -> output:#WS2812#0
- U$618: device output:#WS2812_#0 -> SparkFun-Aesthetics:QWIIC_4MM
- U$619: device output:#0#TX_#0 -> output:250
- U$620: device output:#1#RX_#0 -> output:CHARGE0
- U$621: device output:#4#CIPO_#0 -> output:BOOT0
- U$622: device output:#3#COPI_#0 -> output:#22_#0
- U$623: device output:#2#SCK_#0 -> output:#21_#0
- U$624: device output:#_SCL#7#23#0 -> output:#20_#0
- U$625: device output:#_SDA#6#0 -> output:#19_#0
- U$626: device output:#29#ADC3_#0 -> output:#18_#0
- U$627: device output:#28#ADC2_#0 -> output:#17_#0
- U$628: device output:#27#ADC1_#0 -> output:#16_#0
- U$629: device output:#26#ADC0_#0 -> output:#VUSB_#0
- U$630: device output:#_VUSB#0 -> output:#EN_#0
- U$631: device output:#_EN#0 -> output:#VBATT_#0
- U$632: device output:#_VBATT#0 -> output:#SCL_#0
- U$633: device output:#GND_#0 -> output:#SDA_#0
- U$634: device output:#AREF_#0 -> output:#_#RESET##0
- U$635: device output:#3#3V_#0 -> output:#_3#3V#0
- U$636: device output:##RESET##0 -> output:#_AREF#0
- U$637: device output:#WS2812#0 -> output:#_GND#0
- U$638: device SparkFun-Aesthetics:QWIIC_4MM -> output:#_26#ADC0#0
- U$639: device SparkFun-Aesthetics:SFE_LOGO_NAME_FLAME_.1 -> output:#_27#ADC1#0
- U$640: device output:250 -> output:#_28#ADC2#0
- U$641: device output:CHARGE0 -> output:#_29#ADC3#0
- U$642: device output:BOOT0 -> output:#_NC#0
- U$643: device output:#22_#0 -> output:#_NC#0
- U$644: device output:#21_#0 -> output:PWR0
- U$645: device output:#20_#0 -> output:#I�C#0
- U$646: device output:#19_#0 -> SparkFun-Aesthetics:SFE_LOGO_NAME_.1
- U$647: device output:#18_#0 -> output:THING_PLUS_0
- U$648: device output:#17_#0 -> RP2040:RP2040_10
- U$649: device output:#16_#0 -> ARM1848_DevSummit_2021_Logos_ST3_Stacked#black#jpg (3):ARM1848_DEVSUMMIT_2021_LOGOS_ST3_STACKED#BLACK#JPG
- U$650: device output:#VUSB_#0 -> output:#_16#0
- U$651: device output:#EN_#0 -> output:#_17#0
- U$652: device output:#VBATT_#0 -> output:#_18#0
- U$653: device output:#SCL_#0 -> output:#_19#0
- U$654: device output:#SDA_#0 -> output:#_20#0
- U$655: device output:#_#RESET##0 -> output:#_21#0
- U$656: device output:#_3#3V#0 -> output:#_22#0
- U$657: device output:#_AREF#0 -> output:#WS2812_#0
- U$658: device output:#_GND#0 -> output:#0#TX_#0
- U$659: device output:#_26#ADC0#0 -> output:#1#RX_#0
- U$660: device output:#_27#ADC1#0 -> output:#4#CIPO_#0
- U$661: device output:#_28#ADC2#0 -> output:#3#COPI_#0
- U$662: device output:#_29#ADC3#0 -> output:#2#SCK_#0
- U$663: device output:#_NC#0 -> output:#_SCL#7#23#0
- U$664: device output:#_NC#0 -> output:#_SDA#6#0
- U$665: device output:PWR0 -> output:#29#ADC3_#0
- U$666: device output:#I�C#0 -> output:#28#ADC2_#0
- U$667: device SparkFun-Aesthetics:SFE_LOGO_NAME_.1 -> output:#27#ADC1_#0
- U$668: device output:THING_PLUS_0 -> output:#26#ADC0_#0
- U$669: device output:THING_PLUS0 -> output:#_VUSB#0
- U$670: device RP2040:RP2040_20 -> output:#_EN#0
- U$671: device RP2040:RP2040_10 -> output:#_VBATT#0
- U$672: device output:#_16#0 -> output:#GND_#0
- U$673: device output:#_17#0 -> output:#AREF_#0
- U$674: device output:#_18#0 -> output:#3#3V_#0
- U$675: device output:#_19#0 -> output:##RESET##0
- U$676: device output:#_20#0 -> output:#WS2812#0
- U$677: device output:#_21#0 -> SparkFun-Aesthetics:QWIIC_4MM
- U$678: device output:#_22#0 -> output:250
- U$679: device output:#WS2812_#0 -> output:CHARGE0
- U$680: device output:#0#TX_#0 -> output:BOOT0
- U$681: device output:#1#RX_#0 -> output:#22_#0
- U$682: device output:#4#CIPO_#0 -> output:#21_#0
- U$683: device output:#3#COPI_#0 -> output:#20_#0
- U$684: device output:#2#SCK_#0 -> output:#19_#0
- U$685: device output:#_SCL#7#23#0 -> output:#18_#0
- U$686: device output:#_SDA#6#0 -> output:#17_#0
- U$687: device output:#29#ADC3_#0 -> output:#16_#0
- U$688: device output:#28#ADC2_#0 -> output:#VUSB_#0
- U$689: device output:#27#ADC1_#0 -> output:#EN_#0
- U$690: device output:#26#ADC0_#0 -> output:#VBATT_#0
- U$691: device output:#_VUSB#0 -> output:#SCL_#0
- U$692: device output:#_EN#0 -> output:#SDA_#0
- U$693: device output:#_VBATT#0 -> output:#_#RESET##0
- U$694: device output:#GND_#0 -> output:#_3#3V#0
- U$695: device output:#AREF_#0 -> output:#_AREF#0
- U$696: device output:#3#3V_#0 -> output:#_GND#0
- U$697: device output:##RESET##0 -> output:#_26#ADC0#0
- U$698: device output:#WS2812#0 -> output:#_27#ADC1#0
- U$699: device SparkFun-Aesthetics:QWIIC_4MM -> output:#_28#ADC2#0
- U$700: device SparkFun-Aesthetics:SFE_LOGO_NAME_FLAME_.1 -> output:#_29#ADC3#0
- U$701: device output:250 -> output:#_NC#0
- U$702: device output:CHARGE0 -> output:#_NC#0
- U$703: device output:BOOT0 -> output:PWR0
- U$704: device output:#22_#0 -> output:#I�C#0
- U$705: device output:#21_#0 -> SparkFun-Aesthetics:SFE_LOGO_NAME_.1
- U$706: device output:#20_#0 -> output:THING_PLUS_0
- U$707: device output:#19_#0 -> RP2040:RP2040_10
- U$708: device output:#18_#0 -> ARM1848_DevSummit_2021_Logos_ST3_Stacked#black#jpg (3):ARM1848_DEVSUMMIT_2021_LOGOS_ST3_STACKED#BLACK#JPG
- U$71: device output:#1#RX_#0 -> output:#3#COPI_#0
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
